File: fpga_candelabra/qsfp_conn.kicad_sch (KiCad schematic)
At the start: 25 parts, among them J7 QSFP+, U23 PCA9306DC, U24 TXS0104EPW

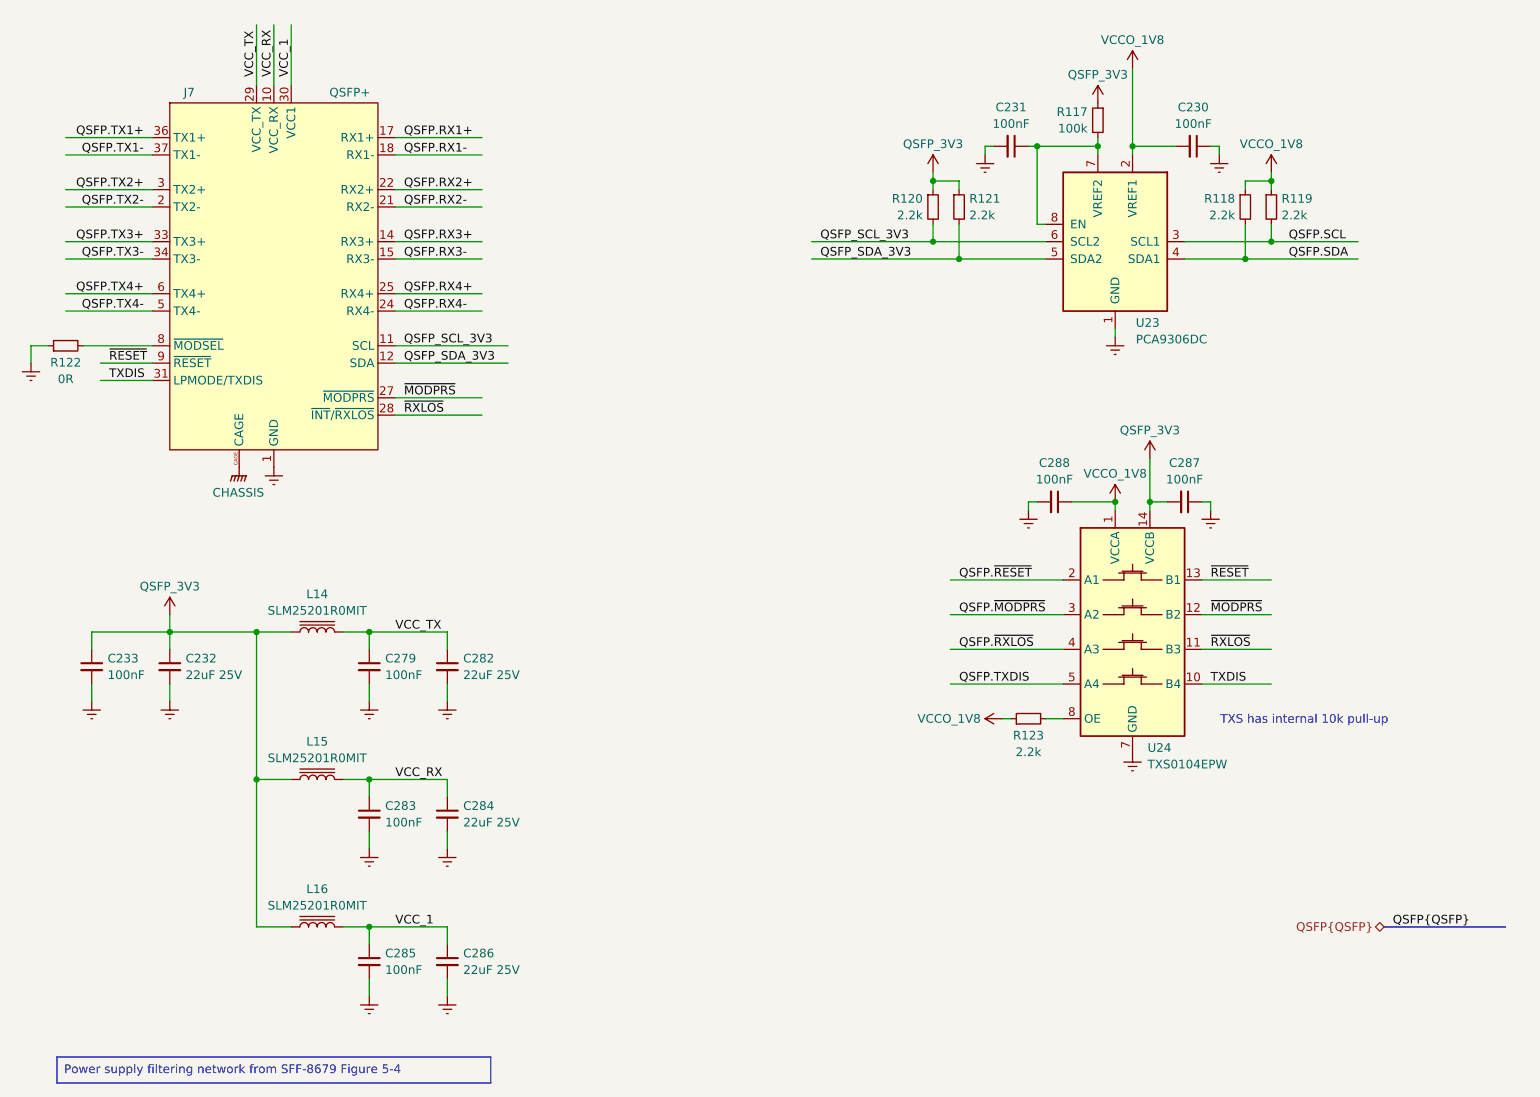
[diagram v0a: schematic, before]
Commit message: fpga_candelabra: major revision
* Finish DDR4 & QSFP+ & PCIe layout
* Change FMC to LPC
* Add mikroBUS extension
* 12V input & PDN updates
* FPGA config updates

Signed-off-by: Yichuan Gao <gaoyichuan000@gmail.com>
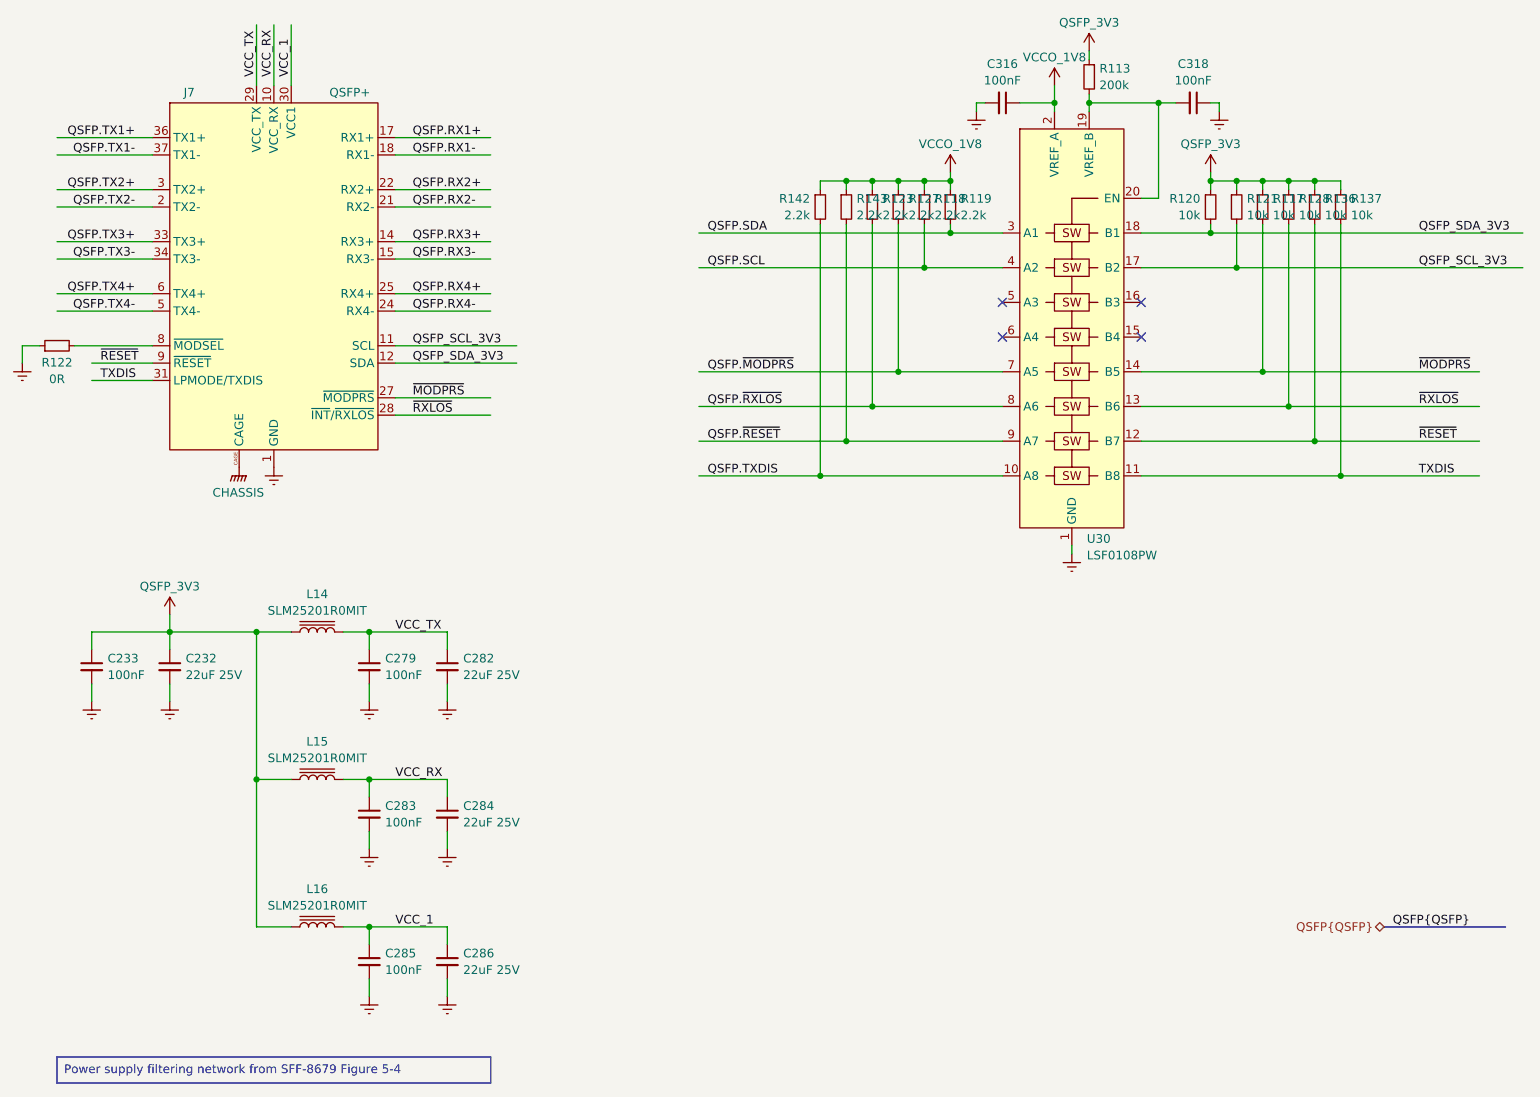
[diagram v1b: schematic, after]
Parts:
- removed C230, C231, C287, C288: 100nF, Capacitor_SMD:C_0402_1005Metric, symbol Device:C_Small
- removed U23: PCA9306DC, Package_SO:VSSOP-8_2.3x2mm_P0.5mm, symbol Interface:PCA9306DC
- removed U24: TXS0104EPW, Package_SO:TSSOP-14_4.4x5mm_P0.65mm, symbol CHIPSAlliance_Logic:TXS0104EPW
- added C316, C318: 100nF, Capacitor_SMD:C_0402_1005Metric, symbol Device:C_Small
- added R113: 200k, Resistor_SMD:R_0402_1005Metric, symbol Device:R_Small
- added R127, R142, R143: 2.2k, Resistor_SMD:R_0402_1005Metric, symbol Device:R_Small
- added R128, R136, R137: 10k, Resistor_SMD:R_0402_1005Metric, symbol Device:R_Small
- added U30: LSF0108PW, Package_SO:TSSOP-20_4.4x6.5mm_P0.65mm, symbol CHIPSAlliance_Logic:LSF0108PW
- R117: value 100k -> 10k
- R120, R121: value 2.2k -> 10k
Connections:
- net Earth: now also C316.2, C318.1, U30.1 (GND)
- net QSFP.SCL: now also R118.2, U30.4 (A2); no longer R119.2
- net QSFP.SDA: now also R119.2, U30.3 (A1); no longer R118.2
- net QSFP.TXDIS: now also R142.2, U30.10 (A8)
- net QSFP.~{MODPRS}: now also R127.2, U30.7 (A5)
- net QSFP.~{RESET}: now also R143.2, U30.9 (A7)
- net QSFP.~{RXLOS}: now also R123.2, U30.8 (A6)
- net QSFP_3V3: now also R113.1, R128.1, R136.1, R137.1
- net QSFP_SCL_3V3: now also R121.2, U30.17 (B2); no longer R120.2
- net QSFP_SDA_3V3: now also R120.2, U30.18 (B1); no longer R121.2
- net TXDIS: now also R137.2, U30.11 (B8)
- net VCCO_1V8: now also C316.1, R127.1, R142.1, R143.1, U30.2 (VREF_A)
- net ~{MODPRS}: now also R117.2, U30.14 (B5)
- net ~{RESET}: now also R136.2, U30.12 (B7)
- net ~{RXLOS}: now also R128.2, U30.13 (B6)
- new net: C318.2, R113.2, U30.19 (VREF_B), U30.20 (EN)
- no-connect marks 0 -> 4
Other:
- note removed: "TXS has internal 10k pull-up"
- moved on the sheet: R118, R119, R120, R121, R122

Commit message: fpga_candelabra: sch & layout v0.5, pass basic ERC & DRC
Signed-off-by: Yichuan Gao <gaoyichuan000@gmail.com>
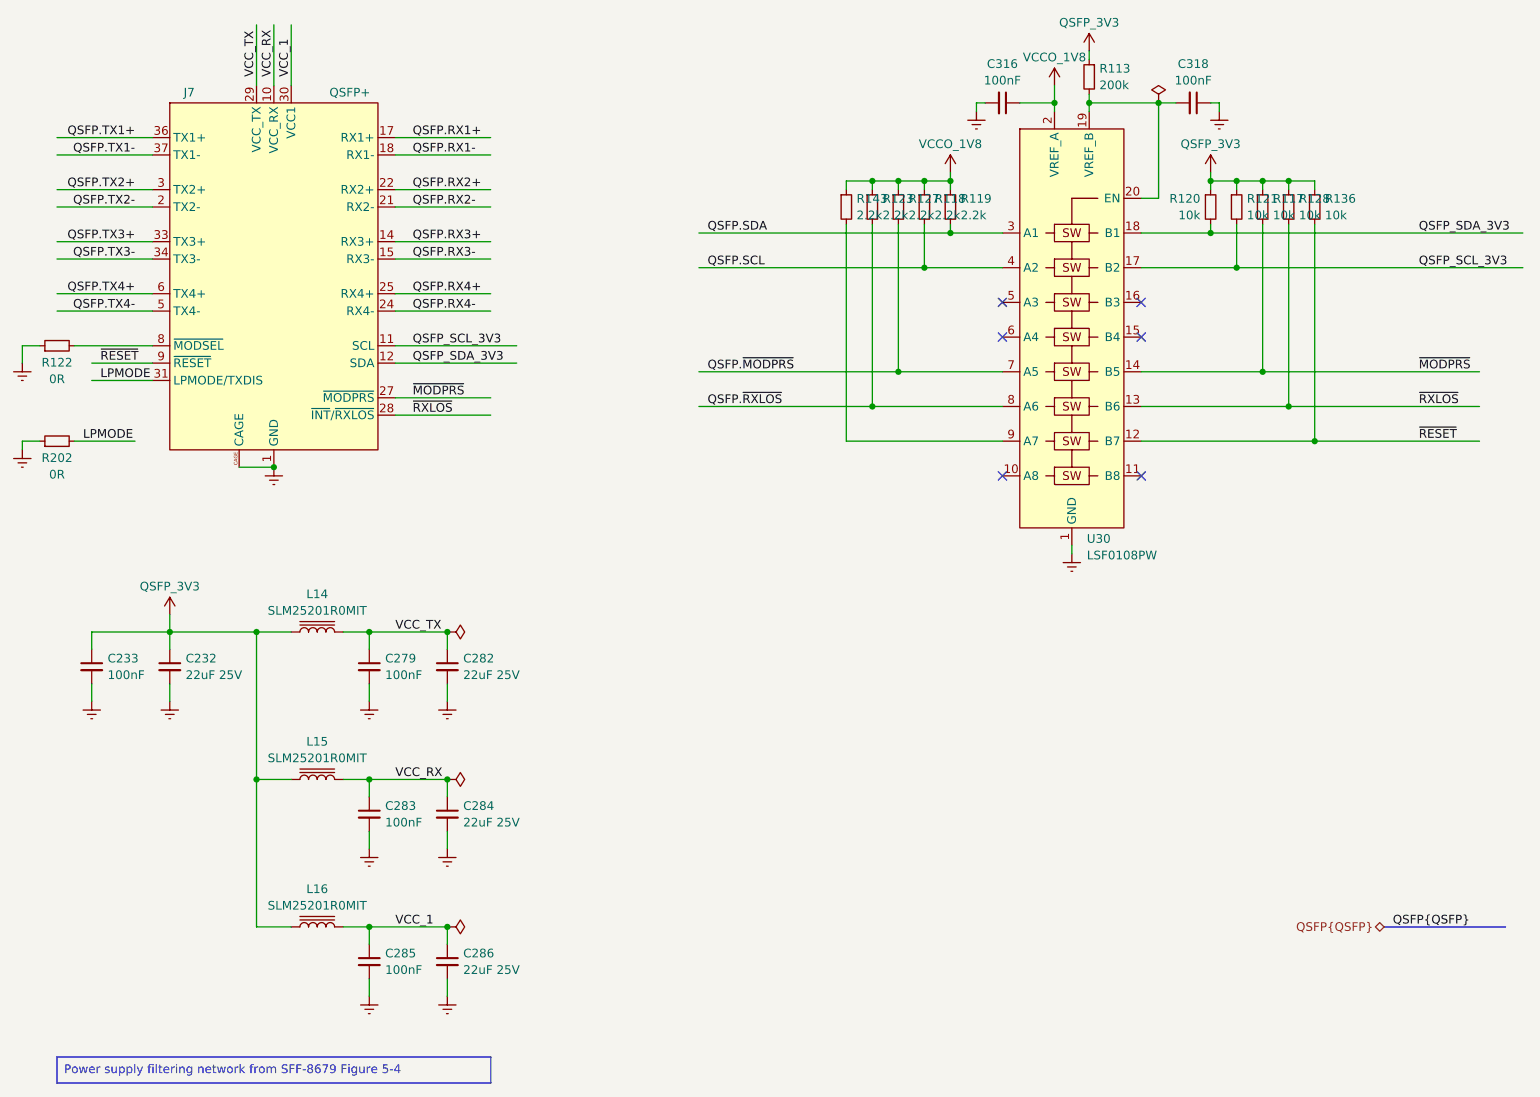
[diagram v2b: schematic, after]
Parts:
- removed R137: 10k, Resistor_SMD:R_0402_1005Metric, symbol Device:R_Small
- removed R142: 2.2k, Resistor_SMD:R_0402_1005Metric, symbol Device:R_Small
- added R202: 0R, Resistor_SMD:R_0402_1005Metric, symbol Device:R_Small
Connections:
- net CHASSIS is gone; now on net Earth: J7.CAGE
- net Earth: now also R202.1
- net QSFP.TXDIS: no longer names the net of U30.10 (A8)
- net QSFP.~{RESET}: no longer names the net of R143.2, U30.9 (A7)
- net TXDIS: no longer names the net of U30.11 (B8)
- net TXDIS: no longer J7.31 (LPMODE/TXDIS)
- new net LPMODE: J7.31 (LPMODE/TXDIS), R202.2
- no-connect marks 4 -> 6

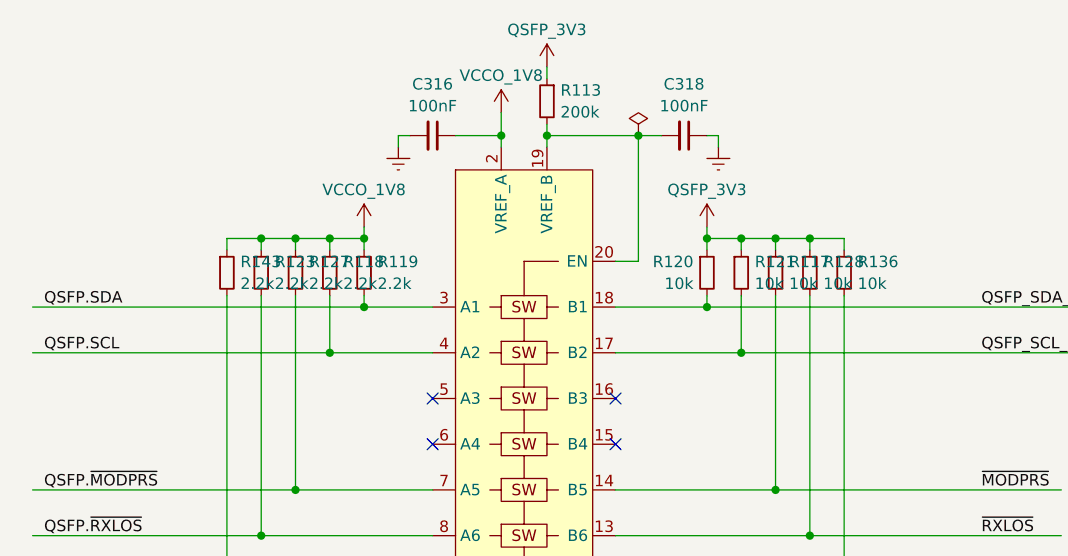
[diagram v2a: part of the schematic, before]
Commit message: fpga_candelabra: more bugfixes & improvements for rev 0.2.0
- Add Digilent JTAG-SMT2-NC onboard
- Add fan controller & 4pin fan header
- Use 9pin header for USB2.0
- Misc fixes for structure

Signed-off-by: Yichuan Gao <gaoyichuan000@gmail.com>
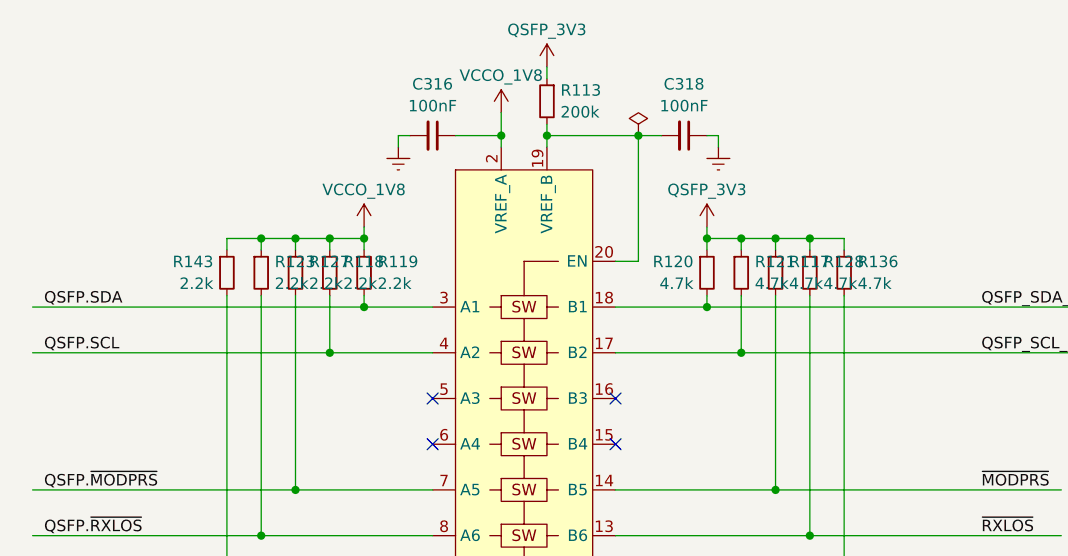
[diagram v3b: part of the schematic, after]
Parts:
- R117, R120, R121, R128, R136: value 10k -> 4.7k
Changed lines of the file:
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@@
 	(label "QSFP.RX4-"
 		(at 109.22 67.31 0)
-		(fields_autoplaced yes)
 		(effects
 			(font
@@
 	(label "VCC_RX"
 		(at 88.9 33.02 90)
-		(fields_autoplaced yes)
 		(effects
 			(font
@@
 	(label "QSFP.~{RXLOS}"
 		(at 152.4 81.28 0)
-		(fields_autoplaced yes)
 		(effects
 			(font
@@
 	(label "QSFP.SDA"
 		(at 152.4 55.88 0)
-		(fields_autoplaced yes)
 		(effects
 			(font
@@
 	(label "QSFP.TX1-"
 		(at 68.58 44.45 180)
-		(fields_autoplaced yes)
 		(effects
 			(font
@@
 	(label "QSFP_SCL_3V3"
 		(at 256.54 60.96 0)
-		(fields_autoplaced yes)
 		(effects
 			(font
@@
 	(label "QSFP.RX3-"
 		(at 109.22 59.69 0)
-		(fields_autoplaced yes)
 		(effects
 			(font
@@
 	(label "QSFP.RX2-"
 		(at 109.22 52.07 0)
-		(fields_autoplaced yes)
 		(effects
 			(font
@@
 	(label "VCC_1"
 		(at 106.68 157.48 0)
-		(fields_autoplaced yes)
 		(effects
 			(font
@@
 	(label "QSFP.~{MODPRS}"
 		(at 152.4 76.2 0)
-		(fields_autoplaced yes)
 		(effects
 			(font
@@
 	(label "QSFP.SCL"
 		(at 152.4 60.96 0)
-		(fields_autoplaced yes)
 		(effects
 			(font
@@
 	(label "~{RXLOS}"
 		(at 256.54 81.28 0)
-		(fields_autoplaced yes)
 		(effects
 			(font
@@
 	(label "QSFP_SCL_3V3"
 		(at 109.22 72.39 0)
-		(fields_autoplaced yes)
 		(effects
 			(font
@@
 	(label "QSFP.RX2+"
 		(at 109.22 49.53 0)
-		(fields_autoplaced yes)
 		(effects
 			(font
@@
 	(label "~{MODPRS}"
 		(at 109.22 80.01 0)
-		(fields_autoplaced yes)
 		(effects
 			(font
@@
 	(label "~{RESET}"
 		(at 63.5 74.93 0)
-		(fields_autoplaced yes)
 		(effects
 			(font
@@
 	(label "QSFP_SDA_3V3"
 		(at 256.54 55.88 0)
-		(fields_autoplaced yes)
 		(effects
 			(font
@@
 	(label "~{RESET}"
 		(at 256.54 86.36 0)
-		(fields_autoplaced yes)
 		(effects
 			(font
@@
 	(label "QSFP.TX2-"
 		(at 68.58 52.07 180)
-		(fields_autoplaced yes)
 		(effects
 			(font
@@
 	(label "QSFP.RX1+"
 		(at 109.22 41.91 0)
-		(fields_autoplaced yes)
 		(effects
 			(font
@@
 	(label "QSFP_SDA_3V3"
 		(at 109.22 74.93 0)
-		(fields_autoplaced yes)
 		(effects
 			(font
@@
 	(label "LPMODE"
 		(at 60.96 86.36 0)
-		(fields_autoplaced yes)
 		(effects
 			(font
@@
 	(label "LPMODE"
 		(at 63.5 77.47 0)
-		(fields_autoplaced yes)
 		(effects
 			(font
@@
 	(label "QSFP.TX4-"
 		(at 68.58 67.31 180)
-		(fields_autoplaced yes)
 		(effects
 			(font
@@
 	(label "QSFP{QSFP}"
 		(at 252.73 157.48 0)
-		(fields_autoplaced yes)
 		(effects
 			(font
@@
 	(label "~{RXLOS}"
 		(at 109.22 82.55 0)
-		(fields_autoplaced yes)
 		(effects
 			(font
@@
 	(label "VCC_RX"
 		(at 106.68 135.89 0)
-		(fields_autoplaced yes)
 		(effects
 			(font
@@
 	(label "QSFP.TX3+"
 		(at 68.58 57.15 180)
-		(fields_autoplaced yes)
 		(effects
 			(font
@@
 	(label "QSFP.RX1-"
 		(at 109.22 44.45 0)
-		(fields_autoplaced yes)
 		(effects
 			(font
@@
 	(label "VCC_TX"
 		(at 106.68 114.3 0)
-		(fields_autoplaced yes)
 		(effects
 			(font
@@
 	(label "QSFP.TX4+"
 		(at 68.58 64.77 180)
-		(fields_autoplaced yes)
 		(effects
 			(font
@@
 	(label "QSFP.RX4+"
 		(at 109.22 64.77 0)
-		(fields_autoplaced yes)
 		(effects
 			(font
@@
 	(label "QSFP.TX3-"
 		(at 68.58 59.69 180)
-		(fields_autoplaced yes)
 		(effects
 			(font
@@
 	(label "QSFP.TX1+"
 		(at 68.58 41.91 180)
-		(fields_autoplaced yes)
 		(effects
 			(font
@@
 	(label "~{MODPRS}"
 		(at 256.54 76.2 0)
-		(fields_autoplaced yes)
 		(effects
 			(font
@@
 	(label "VCC_TX"
 		(at 86.36 33.02 90)
-		(fields_autoplaced yes)
 		(effects
 			(font
@@
 	(label "VCC_1"
 		(at 91.44 33.02 90)
-		(fields_autoplaced yes)
 		(effects
 			(font
@@
 	(label "QSFP.TX2+"
 		(at 68.58 49.53 180)
-		(fields_autoplaced yes)
 		(effects
 			(font
@@
 	(label "QSFP.RX3+"
 		(at 109.22 57.15 0)
-		(fields_autoplaced yes)
 		(effects
 			(font
@@
 		(shape bidirectional)
 		(at 251.46 157.48 180)
-		(fields_autoplaced yes)
 		(effects
 			(font
@@
 		(on_board yes)
 		(dnp no)
-		(fields_autoplaced yes)
 		(property "Reference" "R120"
 			(at 224.5615 50.8578 0)
@@
 			)
 		)
-		(property "Value" "10k"
+		(property "Value" "4.7k"
 			(at 224.5615 53.2821 0)
 			(effects
@@
 			)
 		)
-		(property "Value" "10k"
+		(property "Value" "4.7k"
 			(at 231.3686 53.2821 0)
 			(effects
@@
 		(fields_autoplaced yes)
 		(property "Reference" "R143"
-			(at 174.2186 50.8578 0)
+			(at 171.2215 50.8578 0)
 			(effects
 				(font
 					(size 1.27 1.27)
 				)
-				(justify left)
+				(justify right)
 			)
 		)
 		(property "Value" "2.2k"
-			(at 174.2186 53.2821 0)
+			(at 171.2215 53.2821 0)
 			(effects
 				(font
 					(size 1.27 1.27)
 				)
-				(justify left)
+				(justify right)
 			)
 		)
@@
 			)
 		)
-		(property "Value" "10k"
+		(property "Value" "4.7k"
 			(at 242.7986 53.2821 0)
 			(effects
@@
 			)
 		)
-		(property "Value" "10k"
+		(property "Value" "4.7k"
 			(at 235.1786 53.2821 0)
 			(effects
@@
 			)
 		)
-		(property "Value" "10k"
+		(property "Value" "4.7k"
 			(at 238.9886 53.2821 0)
 			(effects

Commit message: fpga_candelabra: add author & rev to schematics
Signed-off-by: Yichuan Gao <gaoyichuan000@gmail.com>
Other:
- company: (none) -> CHIPS Alliance
- title: (none) -> QSFP+ Connector
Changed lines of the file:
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@@
 	(generator_version "8.0")
 	(paper "A4")
+	(title_block
+		(title "QSFP+ Connector")
+		(date "2025-02-05")
+		(rev "0.2.0")
+		(company "CHIPS Alliance")
+		(comment 1 "Yichuan Gao")
+		(comment 2 "Yichuan Gao")
+	)
 	(junction
 		(at 88.9 90.17)

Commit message: fpga_candelabra: update to kicad 9.0
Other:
- company: CHIPS Alliance -> Sipeed
